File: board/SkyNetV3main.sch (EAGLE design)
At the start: 66 parts, among them IC1 HC_05, IC2 RF4463PRO, IC3 LPC1769, IC4 BCX17, IC5 TPS63001, IC6 MCP73871-2CCI/ML, Q1 32.768KHz, Q2 12MHz, Q3 IRLM6402, Q4 BSS138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

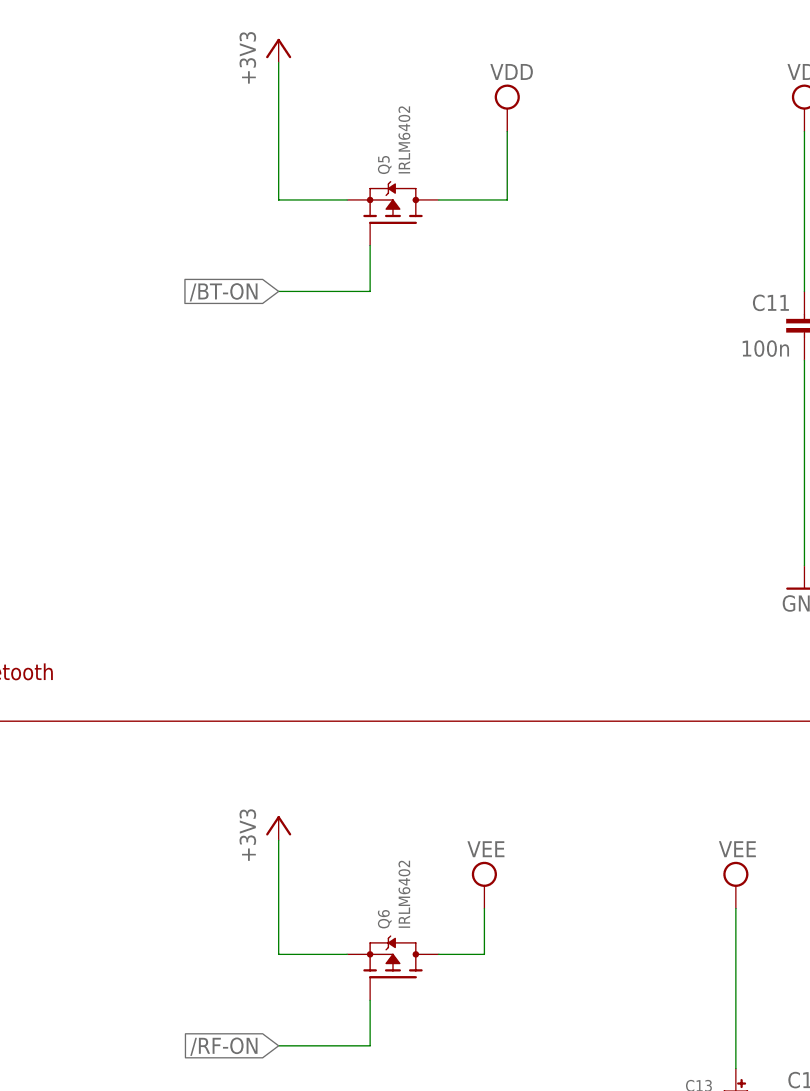
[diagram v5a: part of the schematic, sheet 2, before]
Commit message: added mounting holes
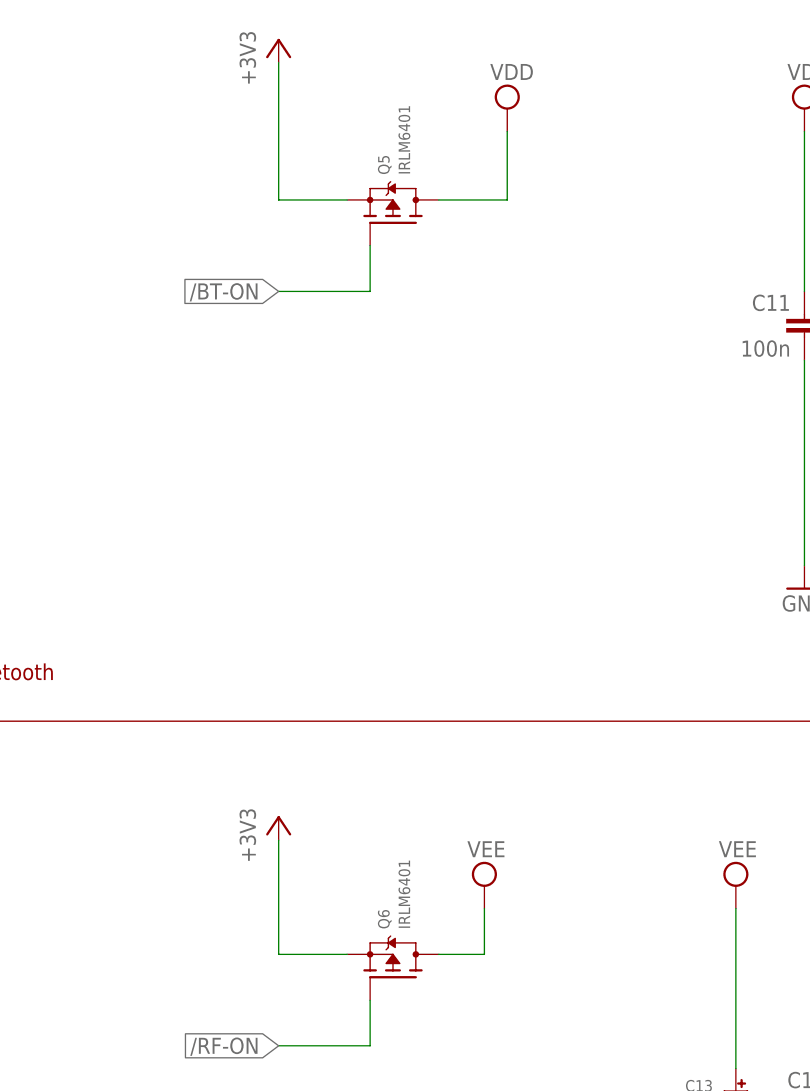
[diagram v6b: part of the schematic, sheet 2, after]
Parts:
- Q3, Q5, Q6: value IRLM6402 -> IRLM6401
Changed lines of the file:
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@@
 <?xml version="1.0" encoding="utf-8"?>
 <!DOCTYPE eagle SYSTEM "eagle.dtd">
-<eagle version="7.1.0">
+<eagle version="7.2.0">
 <drawing>
 <settings>
@@
 <part name="+3V10" library="supply1" deviceset="+3V3" device=""/>
 <part name="GND3" library="supply1" deviceset="GND" device=""/>
-<part name="Q3" library="microbuilder" deviceset="MOSFET-P" device="WIDE" value="IRLM6402"/>
+<part name="Q3" library="microbuilder" deviceset="MOSFET-P" device="WIDE" value="IRLM6401"/>
 <part name="R14" library="rcl" deviceset="R-EU_" device="R0603" value="100k"/>
 <part name="C15" library="rcl" deviceset="C-EU" device="C0603" value="100n"/>
@@
 <part name="SUPPLY4" library="supply2" deviceset="VEE" device=""/>
 <part name="SUPPLY5" library="supply2" deviceset="VDD" device=""/>
-<part name="Q5" library="microbuilder" deviceset="MOSFET-P" device="WIDE" value="IRLM6402"/>
-<part name="Q6" library="microbuilder" deviceset="MOSFET-P" device="WIDE" value="IRLM6402"/>
+<part name="Q5" library="microbuilder" deviceset="MOSFET-P" device="WIDE" value="IRLM6401"/>
+<part name="Q6" library="microbuilder" deviceset="MOSFET-P" device="WIDE" value="IRLM6401"/>
 <part name="SUPPLY6" library="supply2" deviceset="VEE" device=""/>
 <part name="SUPPLY7" library="supply2" deviceset="VDD" device=""/>
